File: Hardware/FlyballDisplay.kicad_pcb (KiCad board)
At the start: 2 copper layers, 106.3 x 49.5 mm, 22 parts, among them U1 TPIC6B595PTH, U2 TPIC6B595PTH, U3 TPIC6B595PTH, U4 TPIC6B595PTH

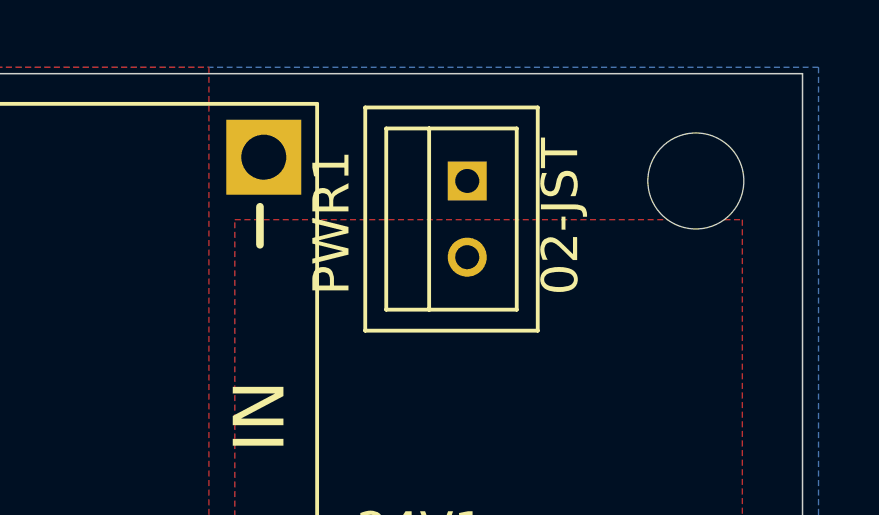
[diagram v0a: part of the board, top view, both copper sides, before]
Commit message: fix: Replaced JST XH header with correct hole size and updated to KiCAD 6
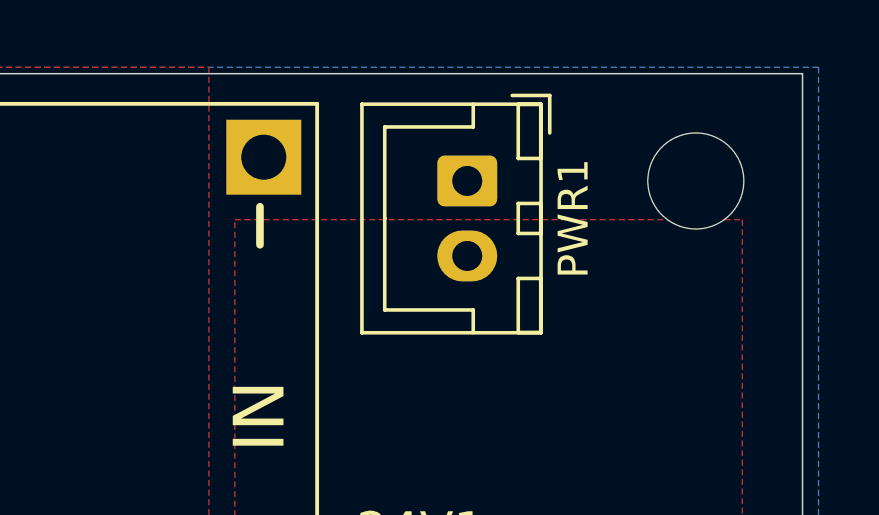
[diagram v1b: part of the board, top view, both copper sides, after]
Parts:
- PWR1: footprint FlyballDisplay:B2B-XH -> Connector_JST:JST_XH_B2B-XH-A_1x02_P2.50mm_Vertical
- moved PWR1 2.54 mm to (190.5, 83.8), turned to -90 degrees
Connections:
- U1 pad 1: Net-(U1-Pad1) -> unconnected-(U1-Pad1)
- U1 pad 20: Net-(U1-Pad20) -> unconnected-(U1-Pad20)
- U2 pad 1: Net-(U2-Pad1) -> unconnected-(U2-Pad1)
- U2 pad 20: Net-(U2-Pad20) -> unconnected-(U2-Pad20)
- U3 pad 1: Net-(U3-Pad1) -> unconnected-(U3-Pad1)
- U3 pad 20: Net-(U3-Pad20) -> unconnected-(U3-Pad20)
- U4 pad 1: Net-(U4-Pad1) -> unconnected-(U4-Pad1)
- U4 pad 18: Net-(U4-Pad18) -> unconnected-(U4-Pad18)
- U4 pad 20: Net-(U4-Pad20) -> unconnected-(U4-Pad20)
- WEMOS1 pad 3V3: Net-(WEMOS1-Pad3V3) -> unconnected-(WEMOS1-Pad3V3)
- WEMOS1 pad A0: Net-(WEMOS1-PadA0) -> unconnected-(WEMOS1-PadA0)
- WEMOS1 pad D0: Net-(WEMOS1-PadD0) -> unconnected-(WEMOS1-PadD0)
- WEMOS1 pad D4: Net-(WEMOS1-PadD4) -> unconnected-(WEMOS1-PadD4)
- WEMOS1 pad D5: Net-(WEMOS1-PadD5) -> unconnected-(WEMOS1-PadD5)
- WEMOS1 pad D6: Net-(WEMOS1-PadD6) -> unconnected-(WEMOS1-PadD6)
- WEMOS1 pad D7: Net-(WEMOS1-PadD7) -> unconnected-(WEMOS1-PadD7)
- WEMOS1 pad RESET: Net-(WEMOS1-PadRESET) -> unconnected-(WEMOS1-PadRESET)
- WEMOS1 pad RX: Net-(WEMOS1-PadRX) -> unconnected-(WEMOS1-PadRX)
- WEMOS1 pad TX: Net-(WEMOS1-PadTX) -> unconnected-(WEMOS1-PadTX)
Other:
- net class Default removed
